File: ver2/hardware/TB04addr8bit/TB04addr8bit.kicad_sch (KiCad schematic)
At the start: 12 parts, among them J1 USB_C_Receptacle_PowerOnly_6P, SW1 SW_SPDT, U15 74HC138, U16 74HC00

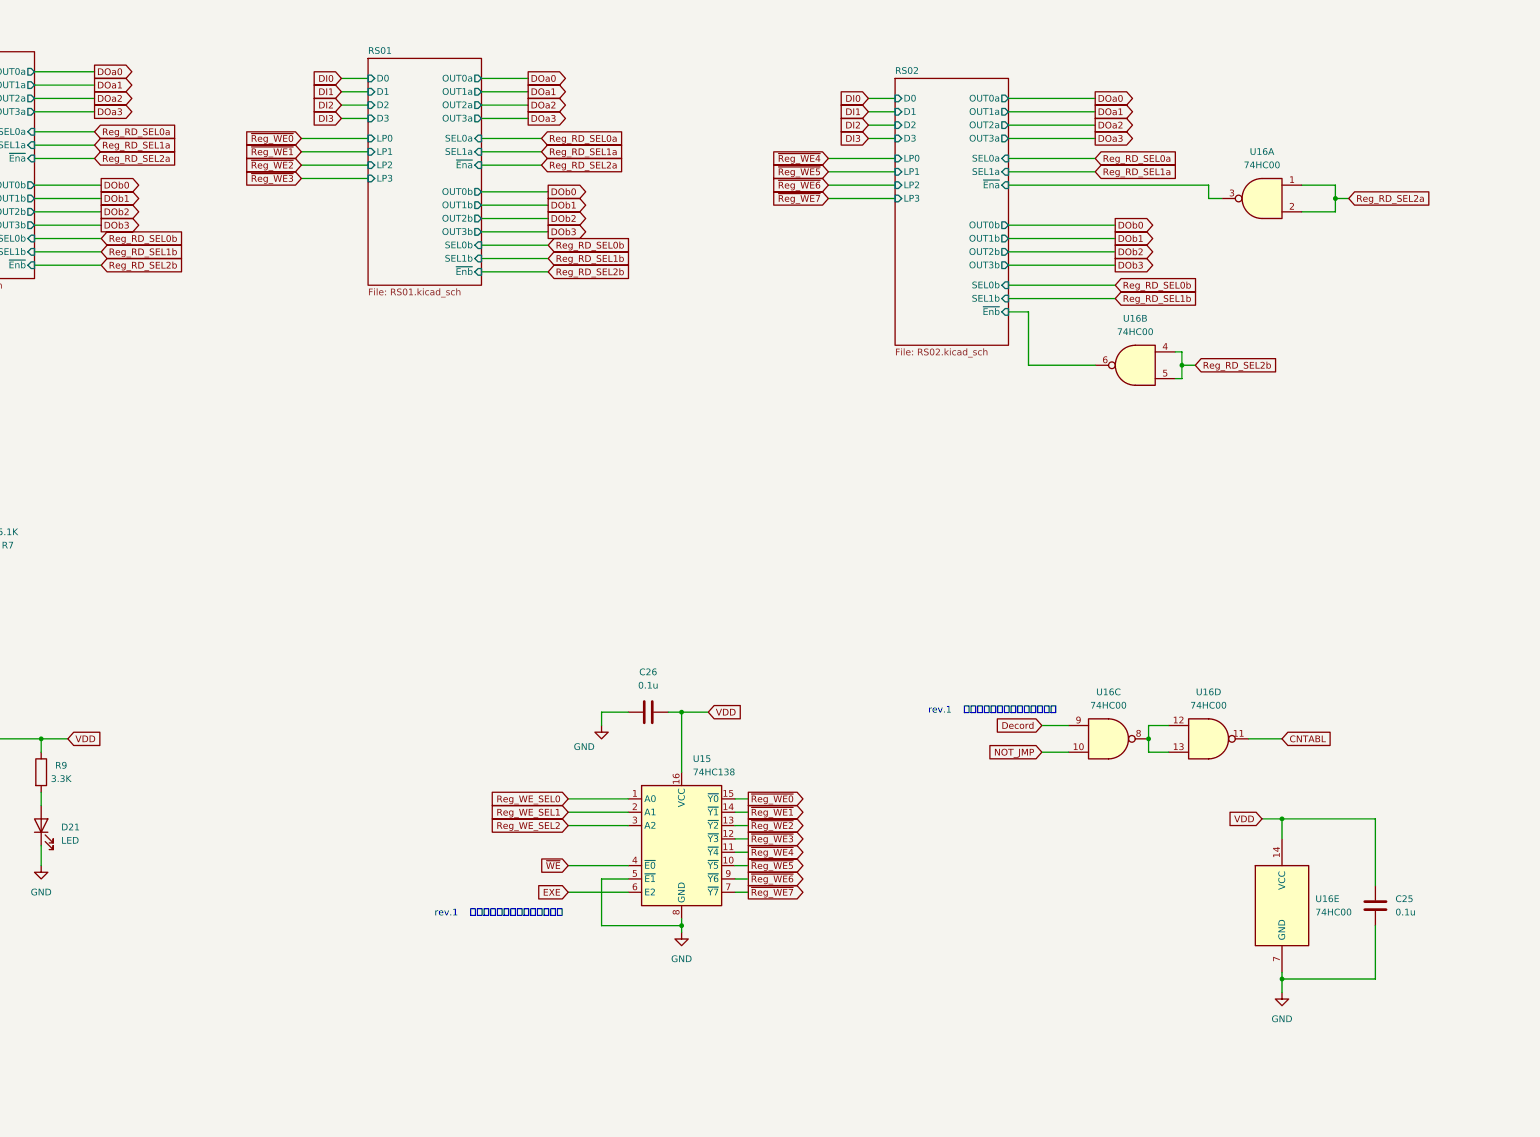
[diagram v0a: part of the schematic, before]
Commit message: ver2: レジスタファイル(RS00/RS01)とルート配線・発振回路定数を追加
- clk_rst: 74HC4060発振のRf=10M/Rs=220K/C=22p×2に確定
- RS00/RS01: R0-R7の具体回路(74HC161×4+74LS253×4)を追加
  ※図面は74LS253だがシンボル都合で実装はHC(74HC253)
- ルート: 書込デコード/読出セレクト/RegAddrSrc MUX/データ入出力の
  外側グルーを配線(DI/DOa/DOb/Reg_WE0-7/sel_a)
- PC_mAddrは作業中(Reg_WE8-11未結線)

Co-Authored-By: Claude Opus 4.8 <noreply@anthropic.com>
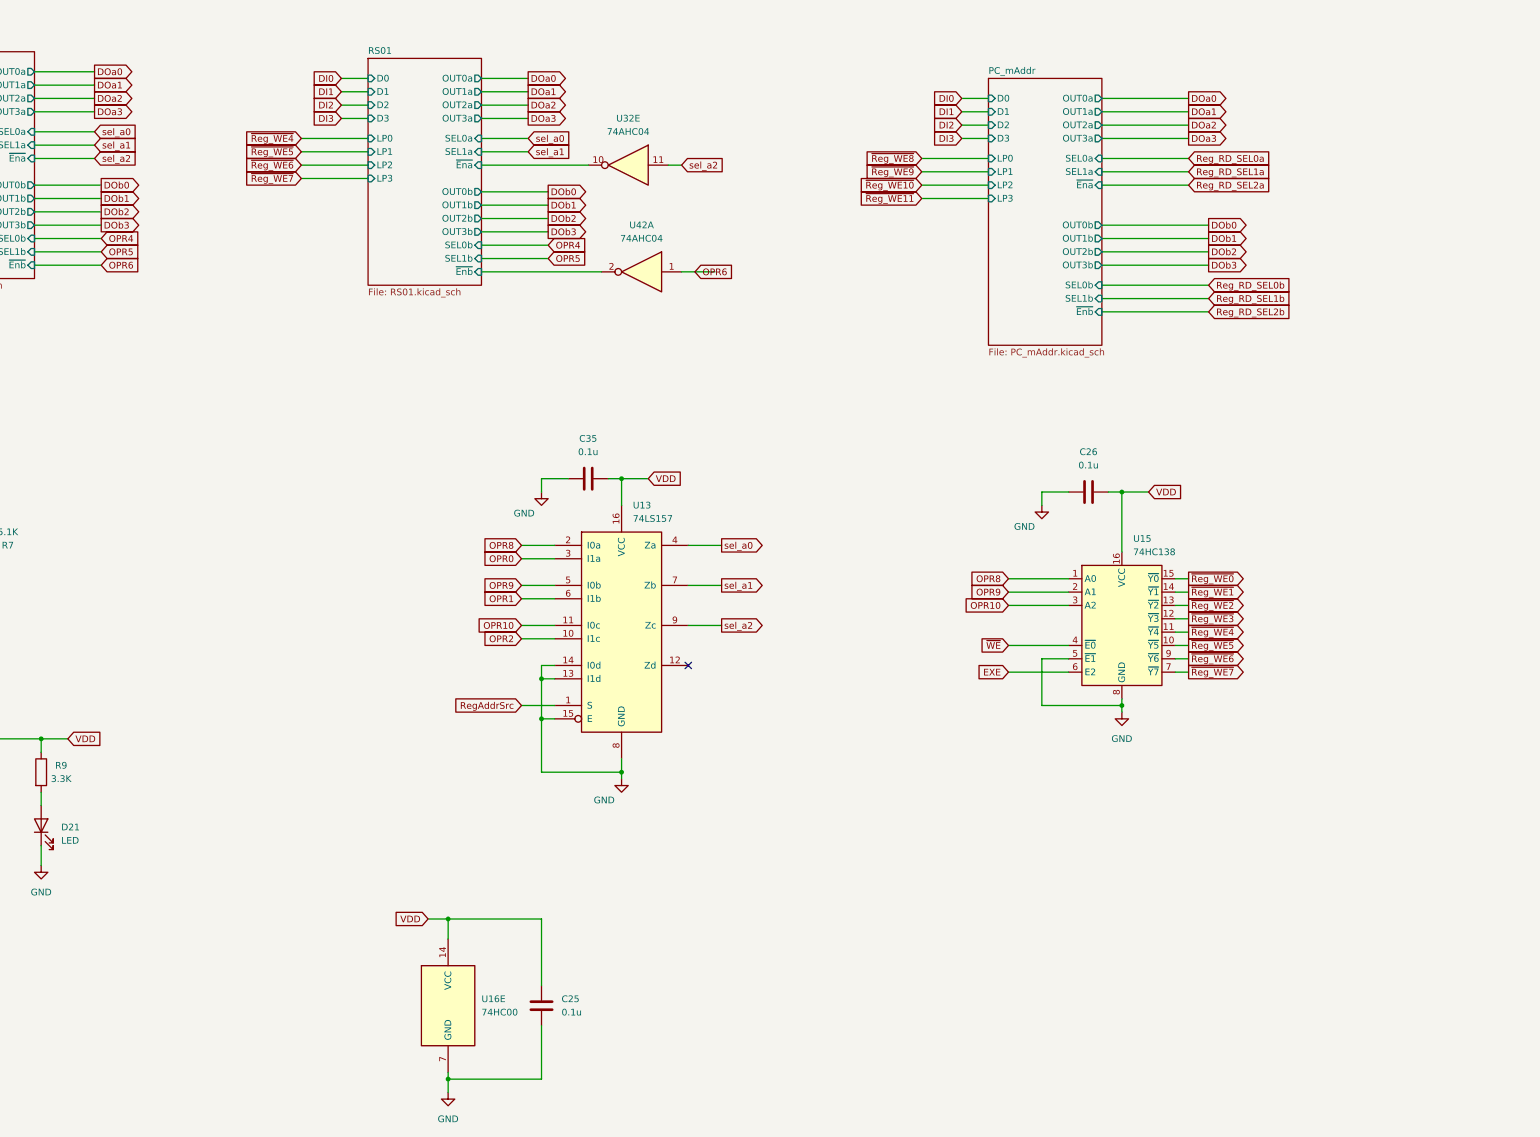
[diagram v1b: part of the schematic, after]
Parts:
- removed unit 3 of U16
- removed unit 4 of U16
- removed unit 2 of U16
- removed unit 1 of U16
- added C35: 0.1u, Capacitor_THT:C_Disc_D4.3mm_W1.9mm_P5.00mm, symbol Device:C
- added U13: 74LS157, symbol 74xx:74LS157
- added U32, U42: 74AHC04, symbol 74xx:74AHC04
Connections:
- net GND: now also C35.2, U13.13 (I1d), U13.14 (I0d), U13.15 (E), U13.8 (GND)
- net VDD: now also C35.1, U13.16 (VCC)
- net Reg_WE_SEL0 renamed OPR8
- net OPR8: now also U13.2 (I0a)
- net Reg_WE_SEL1 renamed OPR9
- net OPR9: now also U13.5 (I0b)
- net Reg_WE_SEL2 renamed OPR10
- net OPR10: now also U13.11 (I0c)
- new net OPR0: U13.3 (I1a)
- new net OPR1: U13.6 (I1b)
- new net OPR2: U13.10 (I1c)
- new net OPR6: U42.1
- new net RS01/~{Ena}: U32.10
- new net RS01/~{Enb}: U42.2
- new net RegAddrSrc: U13.1 (S)
- new net sel_a0: U13.4 (Za)
- new net sel_a1: U13.7 (Zb)
- new net sel_a2: U13.9 (Zc), U32.11
- no-connect marks 5 -> 6
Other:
- sheet RS02 renamed PC_mAddr
- sheet PC_mAddr: file RS02.kicad_sch -> PC_mAddr.kicad_sch
- note removed: "rev.1 タイミングを考慮した結果変更"
- moved on the sheet: C25, C26, U15, U16E

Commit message: ver2: PC_mAddr中心に回路図の配線を更新
7/18のコミット以降の結線作業を反映。部品・ラベルの増減はなく、
配線(wire)とジャンクションの変更のみ。
- PC_mAddr.kicad_sch: 配線36箇所
- sp.kicad_sch / ROM_ALU.kicad_sch / ルートシート: 数箇所ずつ
- TB04addr8bit.kicad_pro: KiCAD 10がERC重要度・last_pathsの
  既定値を追記したもの(設定の書き戻しで設計内容の変化ではない)

なおこの状態のネットリストを ai-review で出力してレビュー済み。
要修正5件と残作業は ver2/DEVLOG.md(2026-08-10)に記録した(未着手)。

Co-Authored-By: Claude Opus 5 <noreply@anthropic.com>
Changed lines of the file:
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@@
 	(global_label "OPR6"
 		(shape input)
-		(at 208.28 71.12 0)
+		(at 212.09 71.12 0)
 		(fields_autoplaced yes)
 		(effects
@@
 		)
 		(property "Intersheetrefs" "${INTERSHEET_REFS}"
-			(at 216.3452 71.12 0)
+			(at 220.1552 71.12 0)
 			(show_name no)
 			(do_not_autoplace no)
